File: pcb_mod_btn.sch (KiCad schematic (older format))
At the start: 50 parts, among them J1 leds_1, J10 leds_2, J11 led_3, J12 btn_3, J13 leds_4, J14 leds_4, J15 leds_4, J16 leds_4, J17 btn_4, J18 leds_5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

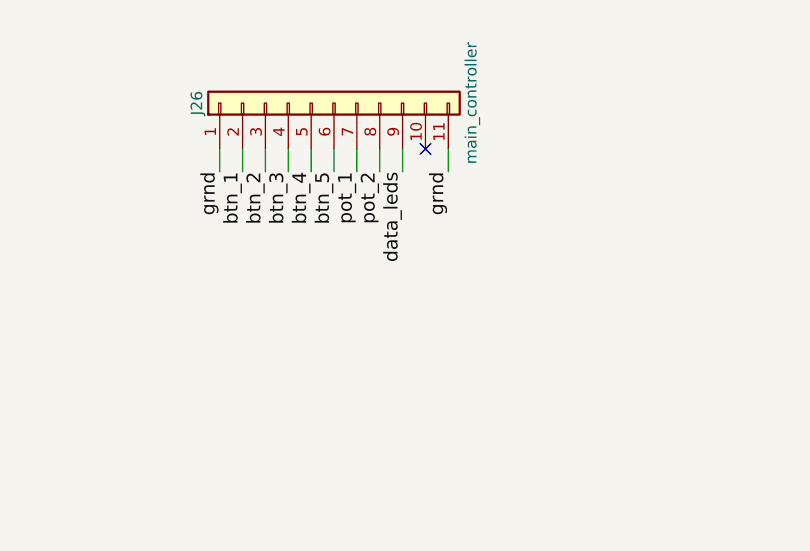
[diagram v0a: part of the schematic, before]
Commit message: footprints para tornillos, modulo botones terminado, todo marcas pin 1 headers
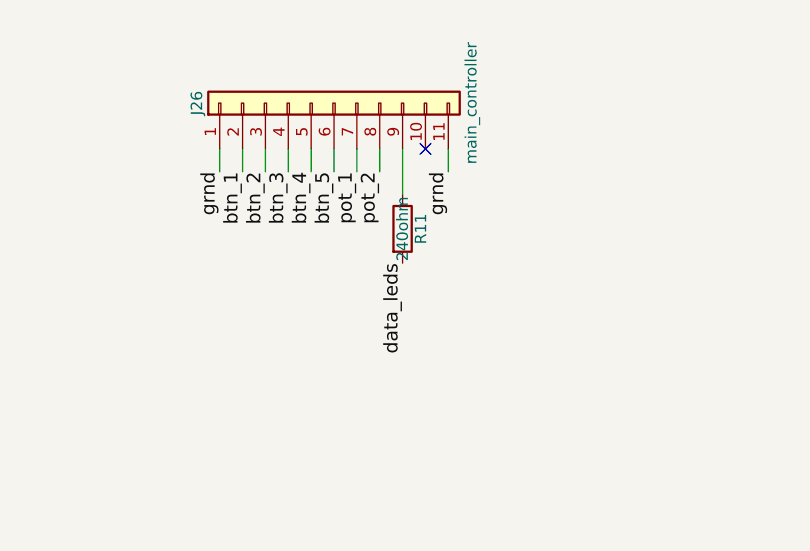
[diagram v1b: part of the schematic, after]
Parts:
- added R11: 240ohm, Resistors_SMD:R_0805_HandSoldering, symbol R
- C1, C2, C3, C4, C5: footprint Capacitors_Tantalum_SMD:CP_Tantalum_Case-T_EIA-3528-12_Hand -> Capacitors_THT:CP_Radial_D8.0mm_P5.00mm
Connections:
- net data_leds: now also R11.2; no longer J26.9 (Pin_9)
- new net: J26.9 (Pin_9), R11.1
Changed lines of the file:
@@
 F 0 "C1" H 1275 1200 50  0000 L CNN
 F 1 "CP" H 1275 1000 50  0000 L CNN
-F 2 "Capacitors_Tantalum_SMD:CP_Tantalum_Case-T_EIA-3528-12_Hand" H 1288 950 50  0001 C CNN
+F 2 "Capacitors_THT:CP_Radial_D8.0mm_P5.00mm" H 1288 950 50  0001 C CNN
 F 3 "" H 1250 1100 50  0001 C CNN
 	1    1250 1100
@@
 F 0 "C2" H 2175 1200 50  0000 L CNN
 F 1 "CP" H 2175 1000 50  0000 L CNN
-F 2 "Capacitors_Tantalum_SMD:CP_Tantalum_Case-T_EIA-3528-12_Hand" H 2188 950 50  0001 C CNN
+F 2 "Capacitors_THT:CP_Radial_D8.0mm_P5.00mm" H 2188 950 50  0001 C CNN
 F 3 "" H 2150 1100 50  0001 C CNN
 	1    2150 1100
@@
 F 0 "C3" H 2675 3550 50  0000 L CNN
 F 1 "CP" H 2675 3350 50  0000 L CNN
-F 2 "Capacitors_Tantalum_SMD:CP_Tantalum_Case-T_EIA-3528-12_Hand" H 2688 3300 50  0001 C CNN
+F 2 "Capacitors_THT:CP_Radial_D8.0mm_P5.00mm" H 2688 3300 50  0001 C CNN
 F 3 "" H 2650 3450 50  0001 C CNN
 	1    2650 3450
@@
 F 0 "C4" H 3375 1250 50  0000 L CNN
 F 1 "CP" H 3375 1050 50  0000 L CNN
-F 2 "Capacitors_Tantalum_SMD:CP_Tantalum_Case-T_EIA-3528-12_Hand" H 3388 1000 50  0001 C CNN
+F 2 "Capacitors_THT:CP_Radial_D8.0mm_P5.00mm" H 3388 1000 50  0001 C CNN
 F 3 "" H 3350 1150 50  0001 C CNN
 	1    3350 1150
@@
 Text Label 8550 1400 3    60   ~ 0
 pot_2
-Text Label 8650 1400 3    60   ~ 0
+Text Label 8650 1800 3    60   ~ 0
 data_leds
 Text Label 7850 1400 3    60   ~ 0
@@
 	8550 1300 8550 1400
 Wire Wire Line
-	8650 1300 8650 1400
+	8650 1300 8650 1500
 Wire Wire Line
 	8850 1300 8850 1400
@@
 F 0 "C5" H 4275 1250 50  0000 L CNN
 F 1 "CP" H 4275 1050 50  0000 L CNN
-F 2 "Capacitors_Tantalum_SMD:CP_Tantalum_Case-T_EIA-3528-12_Hand" H 4288 1000 50  0001 C CNN
+F 2 "Capacitors_THT:CP_Radial_D8.0mm_P5.00mm" H 4288 1000 50  0001 C CNN
 F 3 "" H 4250 1150 50  0001 C CNN
 	1    4250 1150
@@
 Connection ~ 8100 3600
 Connection ~ 7550 3600
+$Comp
+L R R11
+U 1 1 5B23D209
+P 8650 1650
+F 0 "R11" V 8730 1650 50  0000 C CNN
+F 1 "240ohm" V 8650 1650 50  0000 C CNN
+F 2 "Resistors_SMD:R_0805_HandSoldering" V 8580 1650 50  0001 C CNN
+F 3 "" H 8650 1650 50  0001 C CNN
+	1    8650 1650
+	1    0    0    -1
+$EndComp
 $EndSCHEMATC
